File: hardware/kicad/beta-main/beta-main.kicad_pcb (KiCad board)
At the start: 4 copper layers, 77.4 x 158.9 mm, 82 parts, among them J1 AUDIO, J10 Servo Socket, J11 Servo Socket, J12 Servo Socket, J13 Servo Socket, J14 Conn_01x04_Pin, J15 Conn_01x04_Pin, J16 Conn_01x04_Pin, J17 Conn_01x04_Pin, J18 XT60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

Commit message: route usb
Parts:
- moved D1 107.9 mm to (78.0, 90.0), turned to 90 degrees
- moved R12 107.6 mm to (78.0, 94.2), turned to -90 degrees
- moved J21 86.8 mm to (65.3, 115.3), turned to 90 degrees
- moved C12 85.1 mm to (35.2, 41.2)
- moved R4 54.6 mm to (37.8, 66.6), turned to 90 degrees
- moved R5 52.5 mm to (39.3, 66.6), turned to 90 degrees
- moved U4 51.1 mm to (40.7, 61.9), turned to 0 degrees
- moved Q1 48.8 mm to (41.9, 67.1), turned to -90 degrees
- moved R1 45.1 mm to (44.5, 66.6), turned to 90 degrees
- moved U2 44.8 mm to (45.2, 61.9), turned to 180 degrees
- moved R3 43.0 mm to (46.0, 66.6), turned to 90 degrees
- moved R2 40.9 mm to (47.5, 66.6), turned to 90 degrees
- moved U1 25.6 mm to (82.9, 67.3)
- moved C15 2.64 mm to (127.8, 115.5)
- moved C1 2.40 mm to (96.4, 66.6), turned to 90 degrees
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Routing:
- net /High Speed Serial/USB3-1-TX_N: track 0.00 -> 70.2 mm, vias 0 -> 2
- net /High Speed Serial/USB3-1-TX_P: track 0.00 -> 68.3 mm, vias 0 -> 2
- net /High Speed Serial/USB3-1-D_N: track 0.00 -> 59.4 mm
- net /High Speed Serial/USB3-1-D_P: track 0.00 -> 58.0 mm
- net /MIPI0_D0_P: track 0.00 -> 55.9 mm, vias 0 -> 2
- net /High Speed Serial/USB3-1-RX_N: track 0.00 -> 53.0 mm
- net /High Speed Serial/USB3-1-RX_P: track 0.00 -> 52.1 mm
- net /SCL0: track 0.00 -> 50.8 mm, vias 0 -> 2
- net /SDA0: track 0.00 -> 49.6 mm, vias 0 -> 2
- net /MIPI0_D0_N: track 0.00 -> 49.3 mm, vias 0 -> 2
- net /MIPI0_D1_P: track 0.73 -> 49.6 mm
- net /MIPI0_C_P: track 0.00 -> 48.5 mm
- net /MIPI0_C_N: track 0.00 -> 48.5 mm
- net /MIPI0_D1_N: track 0.73 -> 47.9 mm
- net /High Speed Serial/USB3-0-TX_N: track 0.00 -> 39.5 mm
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- added copper zone on B.Cu, net +BATT
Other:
- board text added: "AUDIO OUT"
- board text added: "FANS"
- board text added: "POWER BUT"

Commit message: sync
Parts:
- moved R4 52.6 mm to (90.3, 62.9), turned to -90 degrees
- moved R5 49.6 mm to (88.8, 62.9), turned to -90 degrees
- moved U4 47.0 mm to (87.3, 67.7), turned to 180 degrees
- moved Q1 44.6 mm to (86.2, 62.4), turned to 90 degrees
- moved R1 39.3 mm to (83.6, 62.9), turned to -90 degrees
- moved U2 38.1 mm to (82.8, 67.7), turned to 0 degrees
- moved R3 36.3 mm to (82.1, 62.9), turned to -90 degrees
- moved R2 33.3 mm to (80.6, 62.9), turned to -90 degrees
- moved U1 32.7 mm to (73.6, 98.6), turned to -90 degrees
- moved J1 14.4 mm to (65.0, 96.9)
- moved J21 10.1 mm to (65.1, 105.2)
- moved C1 5.86 mm to (100.0, 62.0), turned to 180 degrees
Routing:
- net /Peripherals/SIG: track 13.5 -> 211.9 mm, vias 0 -> 2
- net /Peripherals/SENSOR_SCL: track 0.00 -> 171.8 mm, vias 0 -> 6
- net /Peripherals/SENSOR_SDA: track 0.00 -> 165.3 mm, vias 0 -> 3
- net GND: track 89.3 -> 162.4 mm, vias 37 -> 55
- net /MIPI1_D1_P: track 25.6 -> 67.3 mm
- net /MIPI1_D1_N: track 25.0 -> 66.4 mm
- net /MIPI1_C_P: track 30.8 -> 72.1 mm
- net /MIPI1_C_N: track 30.2 -> 71.3 mm
- net /MIPI1_D0_P: track 23.4 -> 63.7 mm
- net /MIPI1_D0_N: track 22.8 -> 62.8 mm
- net /GPIO/UART3_RX: track 5.12 -> 43.5 mm, vias 0 -> 2
- net /High Speed Serial/USB3-1-RX_P: track 52.1 -> 67.1 mm, vias 0 -> 2
- net /High Speed Serial/USB3-1-RX_N: track 53.0 -> 66.5 mm, vias 0 -> 2
- net /I2S0_WS: track 0.00 -> 12.2 mm, vias 0 -> 2
- net Net-(J1-Pin_1): track 0.00 -> 11.7 mm
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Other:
- board text added: "SERVO CONTROL"

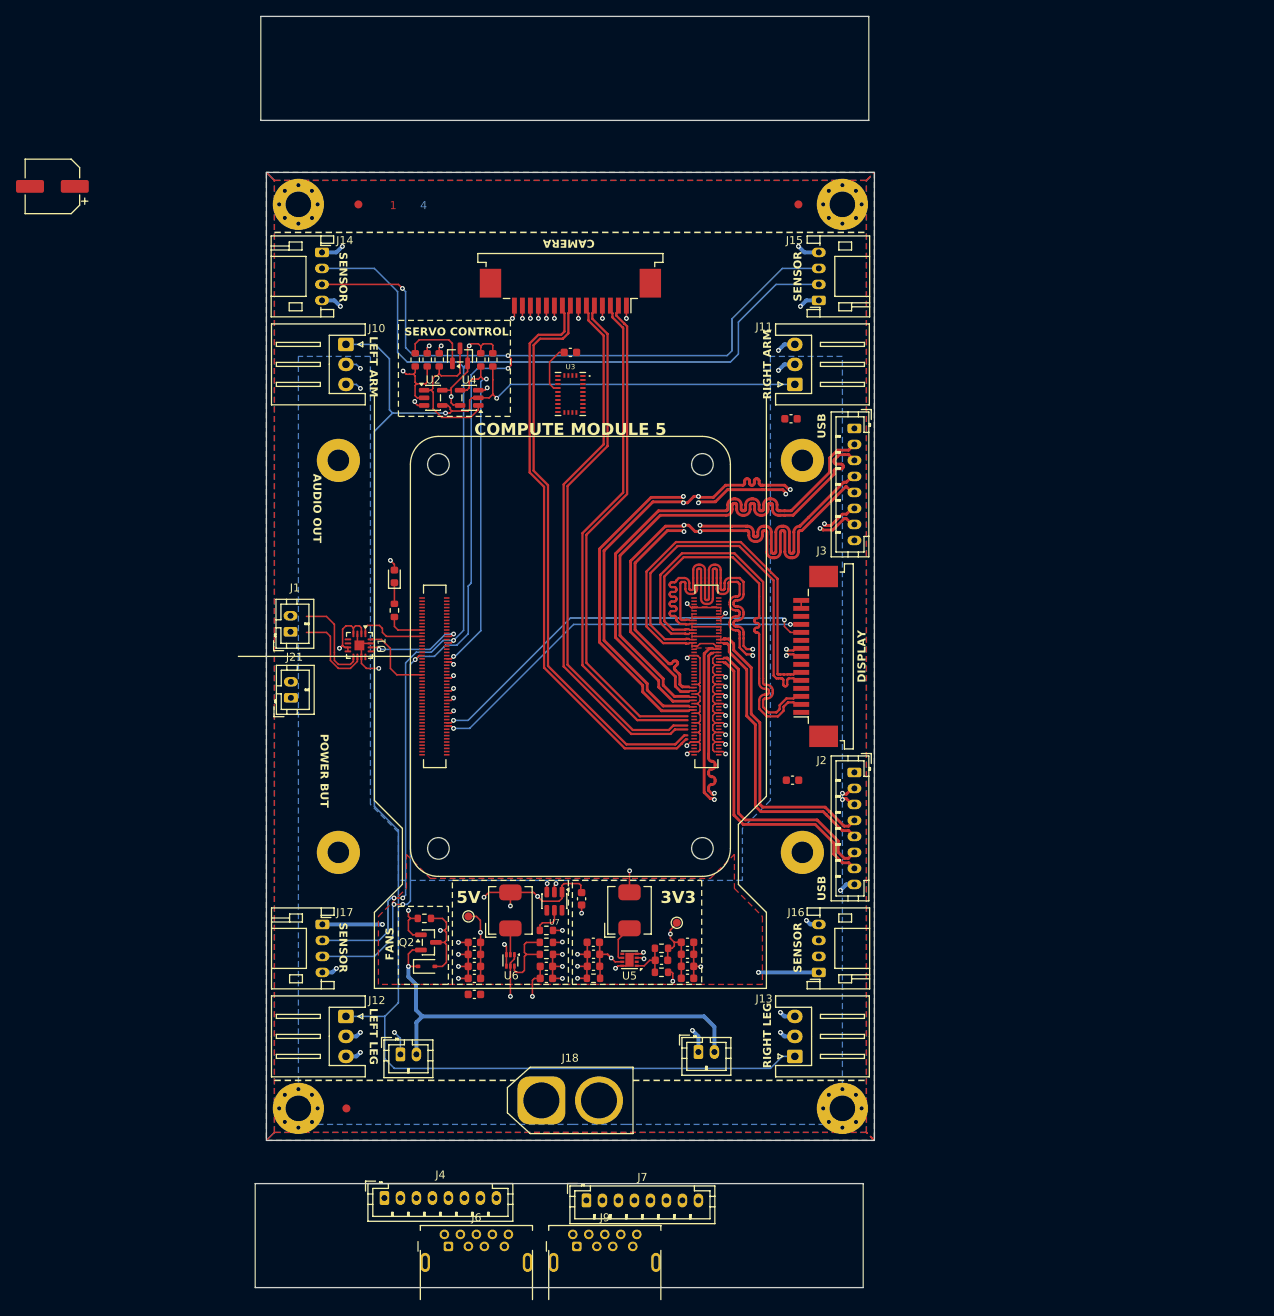
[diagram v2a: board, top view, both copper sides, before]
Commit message: resolve DRC issues and generate fab files
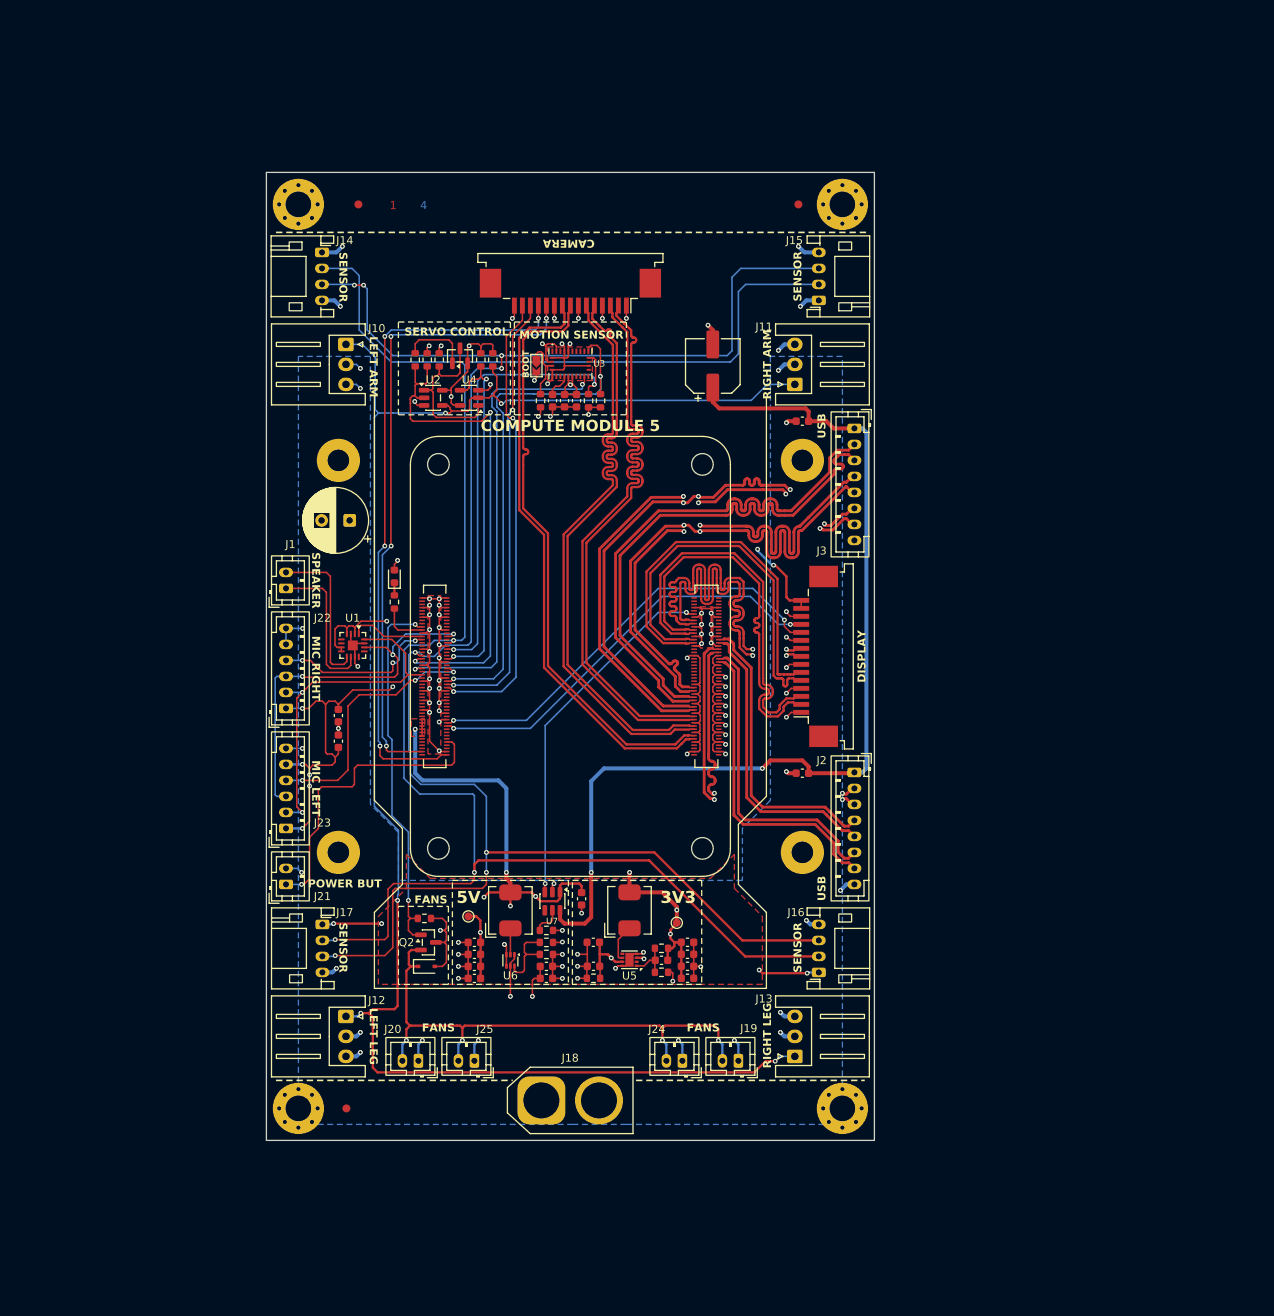
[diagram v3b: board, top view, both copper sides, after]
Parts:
- removed J4, J7: USB3-1, Connector_JST:JST_PH_B8B-PH-K_1x08_P2.00mm_Vertical
- removed J6, J9: USB3_A, BETA:22009L012N1
- added C2: 220u, Capacitor_THT:CP_Radial_D8.0mm_P3.50mm, F.Cu at (72.4, 83.0)
- added C22: 0.1u, Capacitor_SMD:C_0603_1608Metric, F.Cu at (100.8, 68.0)
- added C23: 0.1u, Capacitor_SMD:C_0603_1608Metric, F.Cu at (99.3, 68.0)
- added J22: AUDIO_IN0, Connector_JST:JST_PH_B6B-PH-K_1x06_P2.00mm_Vertical, F.Cu at (64.5, 106.5)
- added J23: AUDIO_IN1, Connector_JST:JST_PH_B6B-PH-K_1x06_P2.00mm_Vertical, F.Cu at (64.5, 121.5)
- added J24: FAN1, Connector_JST:JST_PH_B2B-PH-K_1x02_P2.00mm_Vertical, F.Cu at (114.0, 150.6)
- added J25: FAN1, Connector_JST:JST_PH_B2B-PH-K_1x02_P2.00mm_Vertical, F.Cu at (88.0, 150.6)
- added JP1: SolderJumper_2_Open, BETA:SolderJumper-2, F.Cu at (95.8, 63.6)
- added R14: 10k, Resistor_SMD:R_0603_1608Metric, F.Cu at (96.3, 68.0)
- added R15: 2.2k, Resistor_SMD:R_0603_1608Metric, F.Cu at (102.3, 68.0)
- added R16: 10k, Resistor_SMD:R_0603_1608Metric, F.Cu at (103.8, 68.0)
- C12: footprint Capacitor_SMD:CP_Elec_6.3x5.9 -> Capacitor_SMD:CP_Elec_6.3x7.7
- C7, C8: value 0.1u -> 10u
- moved C12 85.5 mm to (117.8, 63.7), turned to 90 degrees
- moved C7 43.7 mm to (71.0, 107.4), turned to -90 degrees
- moved C8 38.3 mm to (71.0, 110.6), turned to 90 degrees
- moved J21 23.3 mm to (64.5, 128.5)
- moved C3 9.66 mm to (97.0, 138.8), turned to 0 degrees
- moved C1 6.44 mm to (97.8, 68.0), turned to 90 degrees
- moved J1 5.45 mm to (64.5, 91.5)
- moved J19 5.12 mm to (121.0, 150.6), turned to 180 degrees
- moved U3 3.78 mm to (100.0, 63.4), turned to 0 degrees
- moved J20 2.39 mm to (81.0, 150.6), turned to 180 degrees
- moved C15 1.51 mm to (129.0, 114.6)
- moved C21 1.45 mm to (129.0, 70.6)
- moved R12 1.05 mm to (78.0, 93.2)
- moved U1 0.83 mm to (72.8, 98.6)
- moved U7 0.25 mm to (97.8, 130.6)
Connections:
- C7 pad 1: +5V -> +3V3
- C8 pad 1: +BATT -> +3V3
- CM5 pad 27: unconnected-(CM5A-GPIO20-Pad27) -> /I2S0_SDI0
- CM5 pad 46: unconnected-(CM5A-GPIO22-Pad46) -> /I2S0_SDI1
- CM5 pad 47: /GPIO/BNO_RST -> unconnected-(CM5A-GPIO23-Pad47)
- U1 pad 10: Net-(J1-Pin_2) -> Net-(J1-Pin_1)
- U1 pad 9: Net-(J1-Pin_1) -> Net-(J1-Pin_2)
- U3 pad 10: GND -> +3V3
- U3 pad 11: /GPIO/BNO_RST -> +3V3
- U3 pad 18: +3V3 -> unconnected-(U3-~{H_CS}-Pad18)
- U3 pad 26: unconnected-(U3-XOUT32/CLKSEL1-Pad26) -> GND
- U3 pad 4: +3V3 -> Net-(JP1-A)
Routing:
- net VBUS: track 0.00 -> 124.7 mm, vias 0 -> 2
- net GND: track 162.4 -> 260.4 mm, vias 55 -> 92
- net /CAM_GPIO1: track 1.60 -> 83.9 mm, vias 1 -> 4
- net +3V3: track 63.4 -> 144.6 mm, vias 12 -> 28
- net /CAM_GPIO0: track 1.60 -> 79.6 mm, vias 1 -> 4
- net /Peripherals/SENSOR_SDA: track 165.3 -> 234.2 mm
- net /Peripherals/SENSOR_SCL: track 171.8 -> 238.9 mm, vias 6 -> 8
- net /GPIO/I2C2_SDA: track 0.00 -> 65.0 mm, vias 0 -> 2
- net /GPIO/I2C2_SCL: track 0.00 -> 58.8 mm, vias 0 -> 2
- net /GPIO/SDI: track 0.00 -> 58.4 mm, vias 0 -> 2
- net /SDA1: track 1.60 -> 57.6 mm, vias 1 -> 2
- net /SCL1: track 1.60 -> 55.7 mm, vias 1 -> 2
- net /GPIO/UART3_TX: track 10.1 -> 63.6 mm, vias 1 -> 2
- net /VBUS_EN: track 1.08 -> 45.4 mm, vias 1 -> 2
- net /GPIO/FAN_PWM: track 5.42 -> 46.4 mm, vias 1 -> 2
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- added copper zone on F.Cu, net +5V
- removed copper zone on B.Cu, net GND
- removed copper zone on In2.Cu, net GND
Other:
- board size 77.4 x 158.9 mm -> 76 x 121 mm
- board text added: "BOOT"
- board text added: "MIC LEFT"
- board text added: "MIC RIGHT"
- board text added: "MOTION SENSOR"
- board text added: "SPEAKER"
- board text removed: "AUDIO OUT"

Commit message: add final touches, generate rev A fab and step files
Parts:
- added C24: 100u, Capacitor_SMD:CP_Elec_6.3x5.7, F.Cu at (120.0, 52.5)
- added J26: Conn_01x04_Pin, Connector_JST:JST_PH_B4B-PH-K_1x04_P2.00mm_Vertical, F.Cu at (125.0, 150.6)
- added REF**: KiCad-Logo2_5mm_SilkScreen, Symbol:KiCad-Logo2_5mm_SilkScreen, F.Cu at (123.3, 43.3)
- added REF**: Beta-LOGO-3, BETA:Beta-LOGO-3, F.Cu at (104.4, 44.0)
- C11, C14, C17, C19: value 22u -> 10u
- C12: footprint Capacitor_SMD:CP_Elec_6.3x7.7 -> Capacitor_SMD:CP_Elec_6.3x5.7
- C2: value 220u -> 100u; footprint Capacitor_THT:CP_Radial_D8.0mm_P3.50mm -> Capacitor_SMD:CP_Elec_6.3x5.7
- J1: value AUDIO -> Conn_01x02_Pin
- J10, J11, J12, J13: value Servo Socket -> Conn_01x03_Pin; footprint Connector_JST:JST_XH_S3B-XH-A_1x03_P2.50mm_Horizontal -> Connector_JST:JST_XH_B3B-XH-A_1x03_P2.50mm_Vertical
- J14, J15, J16, J17: footprint Connector_JST:JST_PH_S4B-PH-K_1x04_P2.00mm_Horizontal -> Connector_JST:JST_PH_B4B-PH-K_1x04_P2.00mm_Vertical
- J19: value FAN0 -> Conn_01x02_Pin
- J2: value USB3-0 -> Conn_01x08_Pin
- J20, J24, J25: value FAN1 -> Conn_01x02_Pin
- J21: value PWR -> Conn_01x02_Pin
- J22: value AUDIO_IN0 -> Conn_01x06_Pin
- J23: value AUDIO_IN1 -> Conn_01x06_Pin
- J3: value USB3-1 -> Conn_01x08_Pin
- J5: value DSI -> FFC
- J8: value CSI -> FFC
- R12: value 1k -> 100
- R15: value 2.2k -> 10k
- R6: value 100K 1% -> 10k
- moved REF** 113.3 mm to (75.5, 158.1)
- moved FID2 112.9 mm to (128.0, 156.4)
- moved J19 46.0 mm to (75.0, 150.6)
- moved C2 31.4 mm to (80.0, 52.5), turned to 0 degrees
- moved J11 5.92 mm to (134.0, 66.0)
- moved J12 5.92 mm to (66.0, 145.0)
- moved J13 5.92 mm to (134.0, 150.0)
- moved J10 5.42 mm to (66.5, 61.0)
- moved C12 4.30 mm to (120.0, 60.0), turned to 180 degrees
- moved J17 3.45 mm to (65.5, 133.5)
- moved J15 3.45 mm to (134.5, 55.5)
- moved J16 3.40 mm to (134.4, 139.5)
- moved FID1 3.25 mm to (71.2, 41.2)
- moved J14 2.90 mm to (66.0, 49.5)
- moved J20 1.00 mm to (82.0, 150.6)
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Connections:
- CM5 pad 55: unconnected-(CM5A-GPIO14-Pad55) -> /GPIO/BATT_INT
- R12 pad 1: Net-(D1-K) -> Net-(CM5A-LED_nACT)
- R12 pad 2: Net-(CM5A-LED_nACT) -> Net-(D1-K)
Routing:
- net /GPIO/BATT_INT: track 0.00 -> 81.7 mm, vias 0 -> 5
- net +BATT: track 29.4 -> 65.0 mm
- net /Peripherals/SENSOR_SCL: track 238.9 -> 270.0 mm, vias 8 -> 12
- net /Peripherals/SENSOR_SDA: track 234.2 -> 261.9 mm, vias 3 -> 5
- net /Peripherals/SIG: track 215.8 -> 243.0 mm, vias 5 -> 7
- net GND: track 260.4 -> 265.5 mm, vias 92 -> 95
- net Net-(D2-K): track 69.0 -> 64.5 mm
- net +3V3: track 144.6 -> 148.8 mm
- net VBUS: track 124.7 -> 125.6 mm
- net Net-(J1-Pin_2): vias 0 -> 1
- net Net-(J1-Pin_1): vias 0 -> 1
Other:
- board text added: "BATT SIG"
- board text added: "BETA-MAIN REV A 2026-01-19 KOŁO NAUKOWE HUMANOID"
- board text added: "FAN"
- board text added: "KNH"
